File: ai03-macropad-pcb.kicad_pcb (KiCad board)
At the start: 2 copper layers, 69.8 x 94.5 mm, 74 parts, among them J1 Conn_01x06, SW1 SW_Push, U1 ATmega32U4-MU, Y1 16Mhz

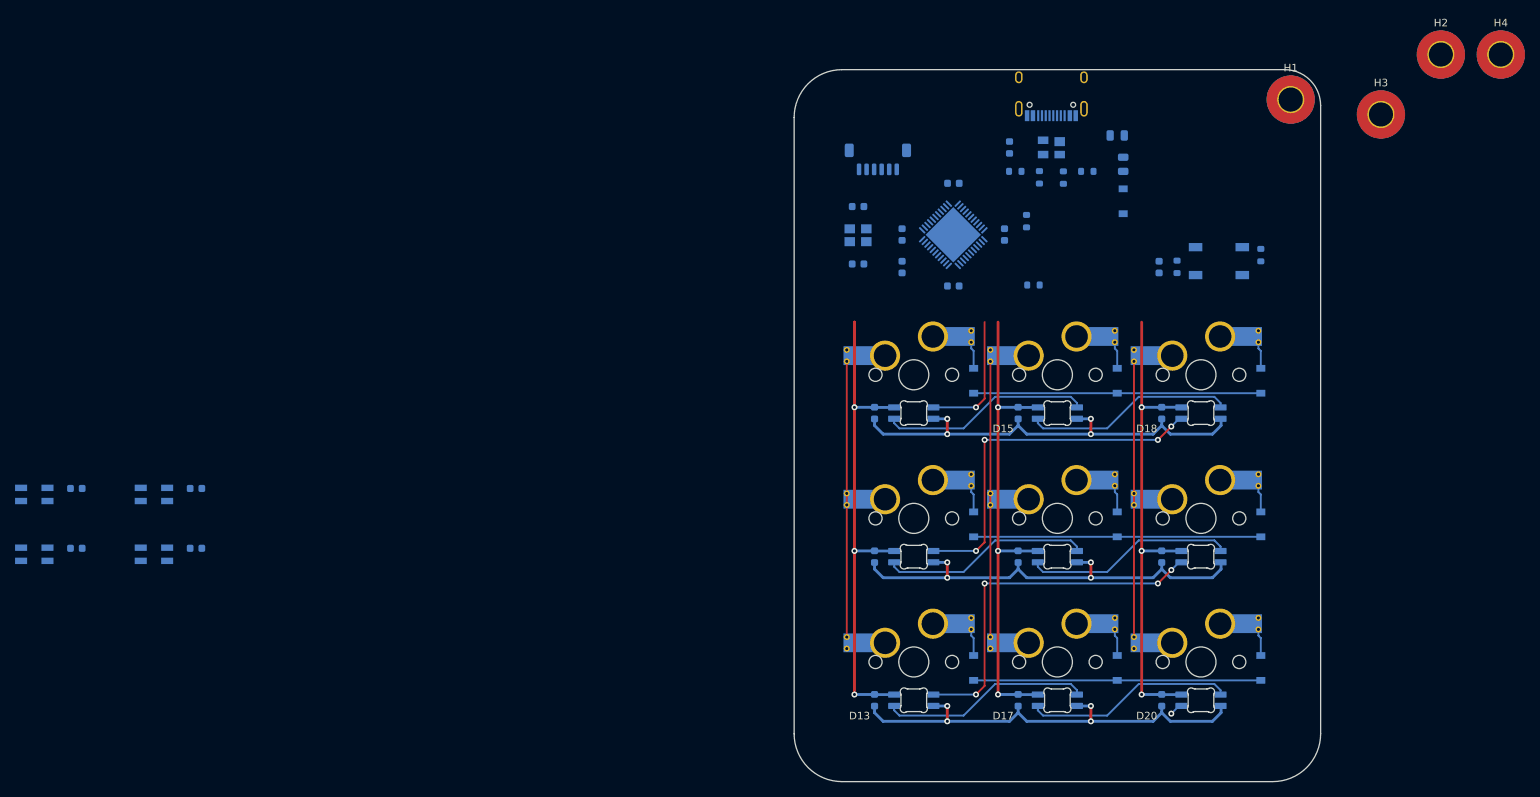
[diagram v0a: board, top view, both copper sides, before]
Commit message: Routing of MCU, USB and BUS Lanes
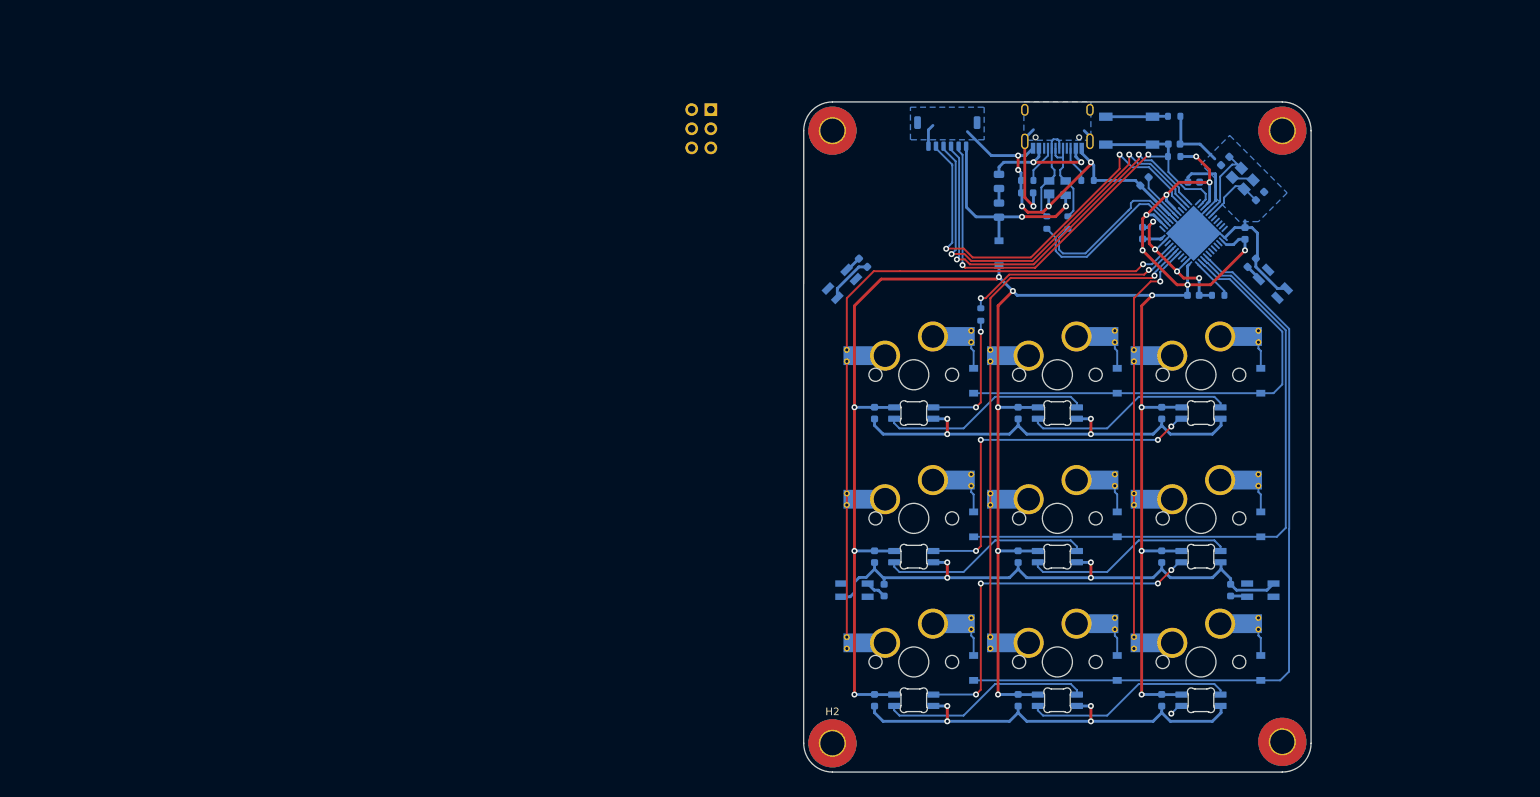
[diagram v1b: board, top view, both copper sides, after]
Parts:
- added REF**: Reset_Pretty-Mask, random-keyboard-parts:Reset_Pretty-Mask, B.Cu at (19.4, 103.9)
- J1: footprint Connector_JST:JST_SH_BM06B-SRSS-TB_1x06-1MP_P1.00mm_Vertical -> Connector_JST:JST_SHL_SM06B-SHLS-TF_1x06-1MP_P1.00mm_Horizontal
- moved D23 151.0 mm to (95.2, 124.5), turned to 315 degrees
- moved D24 146.9 mm to (93.6, 165.1), turned to 0 degrees
- moved C12 143.2 mm to (92.5, 121.7), turned to 45 degrees
- moved C13 137.4 mm to (89.7, 165.1), turned to 90 degrees
- moved H2 121.9 mm to (36.8, 185.4)
- moved D21 110.7 mm to (38.1, 124.5), turned to 225 degrees
- moved D22 108.9 mm to (39.8, 165.1)
- moved C10 108.6 mm to (40.9, 121.7), turned to 315 degrees
- moved C11 107.3 mm to (43.7, 165.1), turned to 90 degrees
- moved H4 95.7 mm to (96.5, 185.2)
- moved H1 60.9 mm to (36.8, 104.1)
- moved C17 53.3 mm to (93.6, 112.8), turned to 225 degrees
- moved Y1 51.6 mm to (91.3, 110.5), turned to 135 degrees
- moved C18 50.6 mm to (88.9, 108.2), turned to 45 degrees
- moved C20 39.3 mm to (84.8, 111.0), turned to 180 degrees
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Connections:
- D22 pad 4: Net-(D22-Pad4) -> Net-(D21-Pad2)
- D23 pad 4: Net-(D21-Pad2) -> Net-(D23-Pad4)
- D24 pad 2: Net-(D22-Pad4) -> Net-(D23-Pad4)
- D24 pad 4: Net-(D23-Pad2) -> Net-(D22-Pad2)
- J1 pad 2: MISO -> SCK
- J1 pad 4: SCK -> MISO
- R5 pad 1: Net-(R5-Pad1) -> D+
- R6 pad 1: Net-(R6-Pad1) -> D-
- U1 pad 3: Net-(R6-Pad1) -> D-
- U1 pad 30: Net-(U1-Pad30) -> ROW2
- U1 pad 31: Net-(U1-Pad31) -> ROW1
- U1 pad 32: Net-(U1-Pad32) -> ROW0
- U1 pad 38: Net-(U1-Pad38) -> COL2
- U1 pad 39: Net-(U1-Pad39) -> COL1
- U1 pad 4: Net-(R5-Pad1) -> D+
- U1 pad 40: Net-(U1-Pad40) -> Net-(R8-Pad2)
- U1 pad 41: Net-(U1-Pad41) -> COL0
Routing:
- net GND: track 179.8 -> 333.5 mm, vias 12 -> 21
- net +5V: track 206.1 -> 329.1 mm, vias 9 -> 19
- net RST: track 0.00 -> 69.9 mm, vias 0 -> 2
- net ROW2: track 38.1 -> 102.8 mm
- net SCK: track 0.00 -> 57.0 mm, vias 0 -> 2
- net MOSI: track 0.00 -> 56.5 mm, vias 0 -> 2
- net MISO: track 0.00 -> 56.0 mm, vias 0 -> 2
- net COL0: track 47.3 -> 100.0 mm, vias 0 -> 1
- net ROW1: track 38.1 -> 83.0 mm
- net D-: track 0.00 -> 36.2 mm
- net D+: track 0.00 -> 34.9 mm
- net COL1: track 43.1 -> 77.4 mm, vias 0 -> 1
- net Net-(R8-Pad2): track 0.00 -> 29.6 mm, vias 0 -> 2
- net VCC: track 0.00 -> 27.1 mm, vias 0 -> 2
- net ROW0: track 38.1 -> 63.1 mm
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- added copper zone on B.Cu, net GND
- added copper zone on B.Cu, net Net-(FB1-Pad2)
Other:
- board size 69.8 x 94.5 mm -> 67.3 x 88.9 mm

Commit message: RevA Routing complete
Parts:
- removed the REF** at (19.4, 103.9)
- added D25: LED, LED_SMD:LED_0603_1608Metric, B.Cu at (75.8, 124.7)
- added G***: LOGO, Logo:rin_small, F.Cu at (54.1, 111.1)
- added G***: LOGO, Logo:jp_logo_hq_11mm, F.Cu at (84.7, 118.0)
- added J2: ICSP, Keebio-Parts:ICSP-Header, F.Cu at (44.5, 115.4)
- added R9: 1k, Resistor_SMD:R_0603_1608Metric, B.Cu at (72.5, 124.7)
- added REF**: Fiducial_1mm_Mask3mm, Fiducial:Fiducial_1mm_Mask3mm, B.Cu at (90.2, 185.4)
- added REF**: Fiducial_1mm_Mask3mm, Fiducial:Fiducial_1mm_Mask3mm, B.Cu at (36.8, 110.5)
- H1, H2, H3, H4: footprint MountingHole:MountingHole_3.2mm_M3_Pad_TopBottom -> MountingHole:MountingHole_3.2mm_M3_DIN965_Pad
- MX1, MX2, MX3, MX4, MX5, MX6, MX7, MX8, MX9: footprint MX_Only:MXOnly-1U-Hotswap-Antishear -> custom_footprints:SW_Hotswap_1.00u
- SW1: footprint random-keyboard-parts:SKQG-1155865 -> Button_Switch_SMD:SW_SPST_CK_KXT3
- moved R8 20.7 mm to (75.9, 121.4), turned to 0 degrees
- moved SW1 5.98 mm to (82.2, 103.8), turned to 180 degrees
- moved D4 1.14 mm to (58.9, 119.3)
- moved C21 1.02 mm to (83.7, 126.0)
- moved R3 0.64 mm to (82.2, 101.6), turned to 0 degrees
- moved R7 0.51 mm to (87.5, 126.0)
- moved H4 0.20 mm to (96.5, 185.4)
- turned C11 to 270 degrees
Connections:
- C14 pad 2: GND -> Net-(C14-Pad2)
- D11 pad 4: RGB1 -> D11
- D12 pad 4: Net-(D12-Pad4) -> D12
- D13 pad 4: Net-(D13-Pad4) -> D13
- D14 pad 4: VCC -> +5V
- D18 pad 2: Net-(D12-Pad4) -> D22
- D19 pad 2: Net-(D13-Pad4) -> D24
- D20 pad 2: RGB2 -> D23
- D21 pad 2: Net-(D21-Pad2) -> D11
- D21 pad 4: RGB2 -> RGB1
- D22 pad 2: Net-(D22-Pad2) -> D12
- D22 pad 4: Net-(D21-Pad2) -> D22
- D23 pad 4: Net-(D23-Pad4) -> D23
- D24 pad 2: Net-(D23-Pad4) -> D13
- D24 pad 4: Net-(D22-Pad2) -> D24
- J1 pad 6: VCC -> +5V
- R3 pad 2: Net-(R3-Pad2) -> Net-(C14-Pad2)
- R5 pad 1: D+ -> Net-(R5-Pad1)
- R6 pad 1: D- -> Net-(R6-Pad1)
- SW1 pad 1: Net-(R3-Pad2) -> Net-(C14-Pad2)
- U1 pad 3: D- -> Net-(R6-Pad1)
- U1 pad 4: D+ -> Net-(R5-Pad1)
- U1 pad 40: Net-(R8-Pad2) -> COL0
- U1 pad 41: COL0 -> Net-(R8-Pad2)
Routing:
- net GND: track 333.5 -> 147.9 mm, vias 21 -> 37
- net +5V: track 329.1 -> 410.9 mm, vias 19 -> 23
- net D23: track 0.00 -> 69.2 mm
- net D22: track 0.00 -> 63.2 mm
- net D13: track 0.00 -> 56.9 mm, vias 0 -> 2
- net Net-(D13-Pad4): track 48.8 -> 0.00 mm, vias 4 -> 0
- net Net-(D12-Pad4): track 48.4 -> 0.00 mm, vias 4 -> 0
- net D11: track 0.00 -> 39.1 mm, vias 0 -> 2
- net VCC: track 27.1 -> 2.05 mm, vias 2 -> 0
- net Net-(R8-Pad2): track 29.6 -> 5.73 mm, vias 2 -> 0
- net D-: track 36.2 -> 13.1 mm
- net RGB1: track 17.4 -> 40.4 mm
- net D+: track 34.9 -> 12.1 mm
- net Net-(R6-Pad1): track 0.00 -> 22.6 mm
- net Net-(R5-Pad1): track 0.00 -> 22.6 mm
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- added copper zone on F.Cu, net GND
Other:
- outline, holes or cut-outs redrawn

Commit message: RevA DRC check
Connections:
- net Net-(R5-Pad1) renamed D_P
- net Net-(R6-Pad1) renamed D_N
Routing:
- net COL1: track 80.4 -> 89.8 mm
- net COL2: track 64.6 -> 71.0 mm
- net COL0: track 103.2 -> 109.6 mm
- net Net-(D8-Pad2): track 6.90 -> 8.99 mm
- net Net-(D7-Pad2): track 6.90 -> 8.99 mm
- net Net-(D6-Pad2): track 6.90 -> 8.99 mm
- net Net-(D5-Pad2): track 6.90 -> 8.99 mm
- net Net-(D10-Pad2): track 6.90 -> 8.99 mm
- net Net-(D3-Pad2): track 6.90 -> 8.99 mm
- net Net-(D1-Pad2): track 6.90 -> 8.99 mm
- net Net-(D2-Pad2): track 7.09 -> 8.99 mm
- net Net-(D9-Pad2): track 8.42 -> 8.99 mm
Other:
- net class Data added: clearance 0.1778, trace_width 0.254, via_dia 0.8, via_drill 0.4
- net class Default: clearance 0.2 -> 0.1778
- net class Power: clearance 0.2 -> 0.1778
- rule trace_clearance: 0.2 -> 0.1778
- rule trace_min: 0.2 -> 0.2032
- rule via_min_size: 0.4 -> 0.3
